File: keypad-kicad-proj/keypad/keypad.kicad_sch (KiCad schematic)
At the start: 13 parts, among them J1 Screw_Terminal_01x02, J2 USB4105-GF-A, U1 ESP32-S3-WROOM-1, U2 TLV75901PDRVT

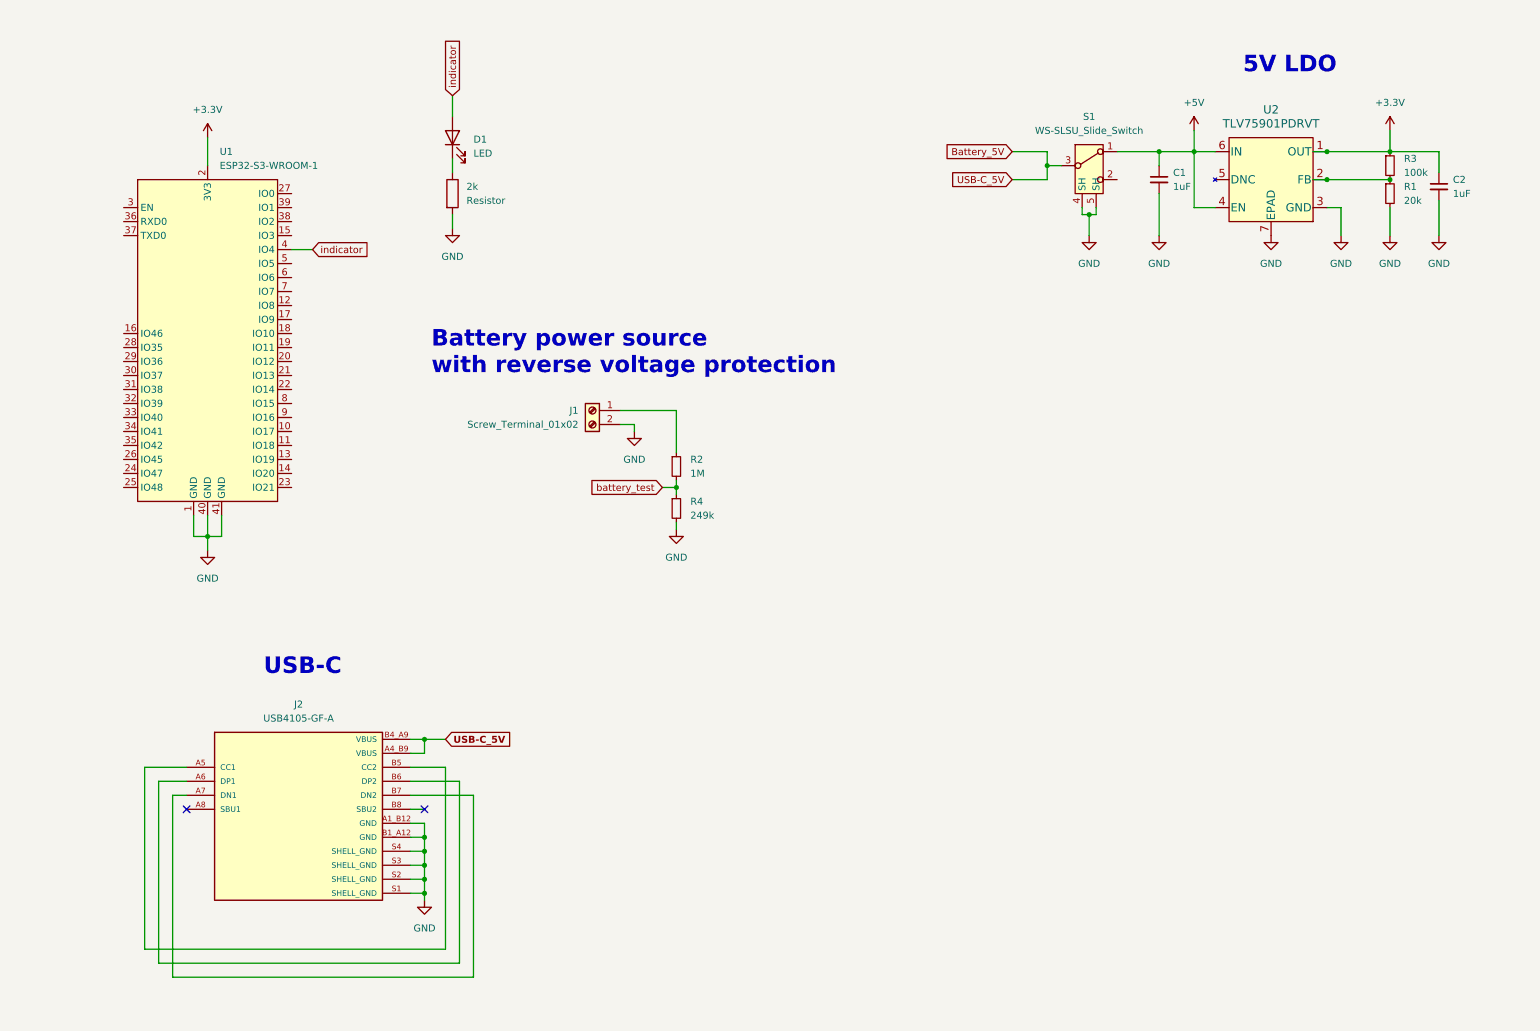
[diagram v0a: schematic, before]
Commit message: add btn matrix & led strip
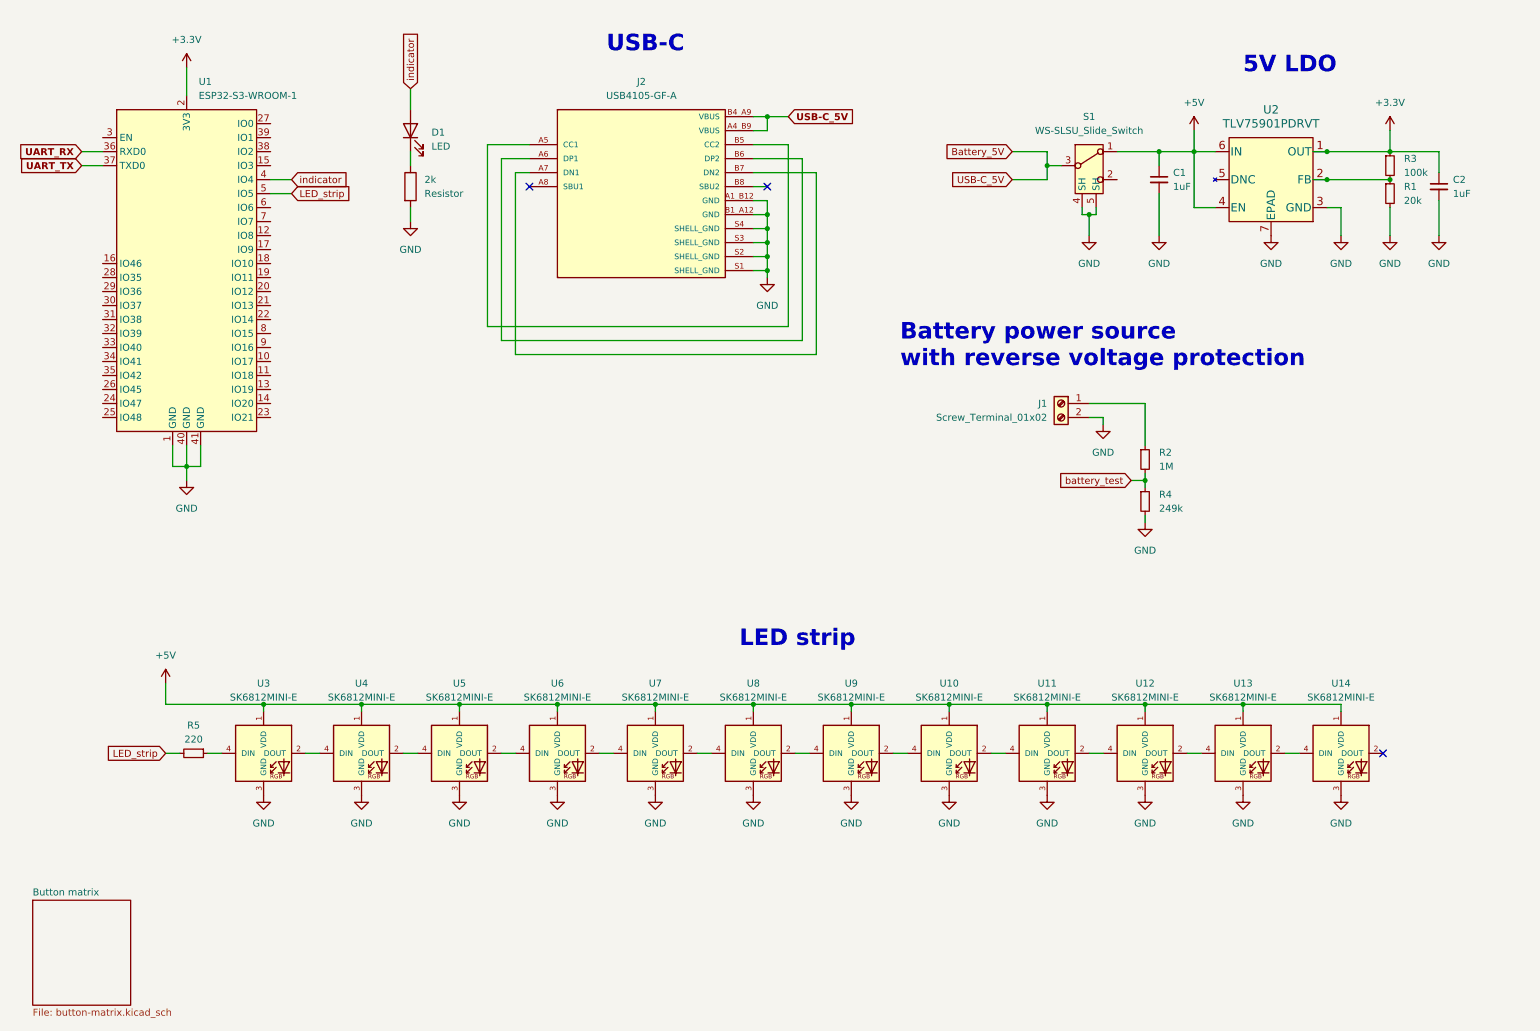
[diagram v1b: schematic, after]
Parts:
- added R5: 220, symbol PutRocketLab_RCL:R_Small
- added U10, U11, U12, U13, U14, U3, U4, U5, U6, U7, U8, U9: SK6812MINI-E, symbol PUT_RocketLab_misc:SK6812MINI-E
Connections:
- net +5V: now also U10.1 (VDD), U11.1 (VDD), U12.1 (VDD), U13.1 (VDD), U14.1 (VDD), U3.1 (VDD), U4.1 (VDD), U5.1 (VDD), U6.1 (VDD), U7.1 (VDD), U8.1 (VDD), U9.1 (VDD)
- net GND: now also U10.3 (GND), U11.3 (GND), U12.3 (GND), U13.3 (GND), U14.3 (GND), U3.3 (GND), U4.3 (GND), U5.3 (GND), U6.3 (GND), U7.3 (GND), U8.3 (GND), U9.3 (GND)
- net UART_RX: now reaches U1.36 (RXD0)
- net UART_TX: now reaches U1.37 (TXD0)
- net LED_strip: now reaches U1.5 (IO5)
- net LED_strip: now also R5.2
- new net: U10.4 (DIN), U9.2 (DOUT)
- new net: U8.2 (DOUT), U9.4 (DIN)
- new net: U7.2 (DOUT), U8.4 (DIN)
- new net: U6.2 (DOUT), U7.4 (DIN)
- new net: U13.2 (DOUT), U14.4 (DIN)
- new net: U12.2 (DOUT), U13.4 (DIN)
- new net: U4.2 (DOUT), U5.4 (DIN)
- new net: U3.2 (DOUT), U4.4 (DIN)
- new net: U5.2 (DOUT), U6.4 (DIN)
- new net: R5.1, U3.4 (DIN)
- new net: U10.2 (DOUT), U11.4 (DIN)
- new net: U11.2 (DOUT), U12.4 (DIN)
- no-connect marks 2 -> 3
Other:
- added sheet Button matrix (button-matrix.kicad_sch)
- note added: "LED strip"
- moved on the sheet: 2k, D1, J1, J2, R2, R4, U1

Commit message: add usb-c interface
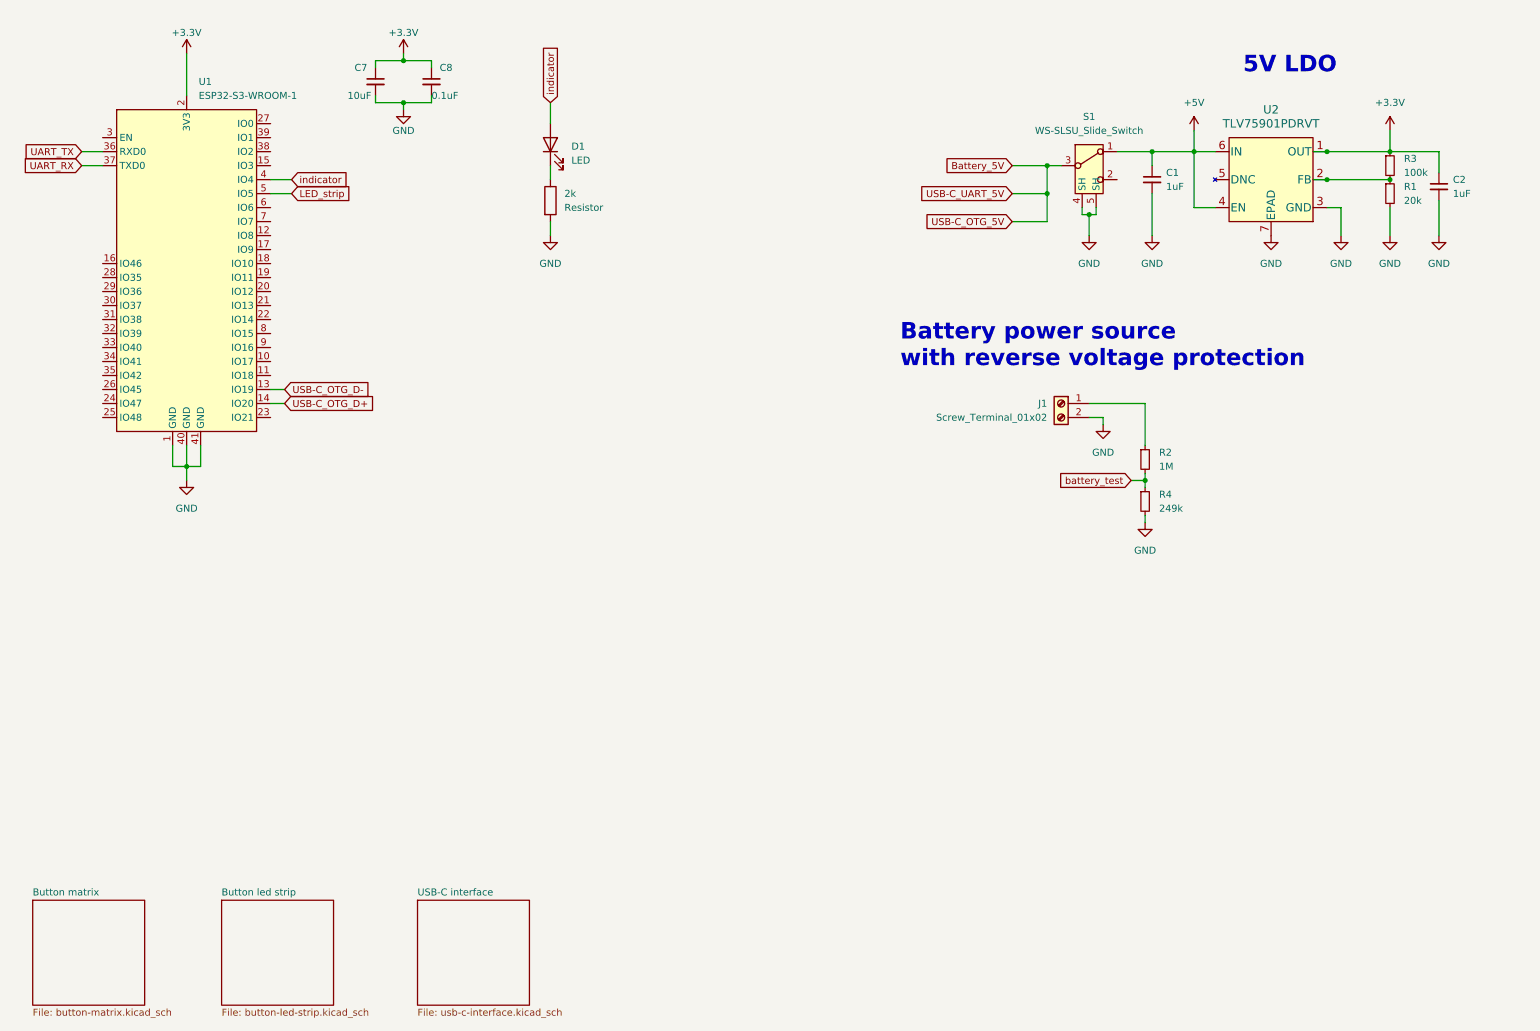
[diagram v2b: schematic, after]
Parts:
- removed J2: USB4105-GF-A, PUTRocketLab_other:GCT_USB4105-GF-A, symbol PUT_RocketLab_connectors:USB4105-GF-A
- removed R5: 220, symbol PutRocketLab_RCL:R_Small
- removed U10, U11, U12, U13, U14, U3, U4, U5, U6, U7, U8, U9: SK6812MINI-E, symbol PUT_RocketLab_misc:SK6812MINI-E
- added C7: 10uF, symbol PutRocketLab_RCL:C_Small
- added C8: 0.1uF, symbol PutRocketLab_RCL:C_Small
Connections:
- net +3V3: now also C7.1, C8.1
- net GND: now also C7.2, C8.2
- net UART_RX: now also U1.37 (TXD0); no longer U1.36 (RXD0)
- net UART_TX: now also U1.36 (RXD0); no longer U1.37 (TXD0)
- net USB-C_OTG_D-: now reaches U1.13 (IO19)
- net USB-C_OTG_D+: now reaches U1.14 (IO20)
- no-connect marks 3 -> 0
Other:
- added sheet Button led strip (button-led-strip.kicad_sch)
- added sheet USB-C interface (usb-c-interface.kicad_sch)
- note removed: "LED strip"
- note removed: "USB-C"
- moved on the sheet: 2k, C1, D1

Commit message: battery source
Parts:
- added D7: D_Small, symbol Device:D_Small
- added Q3: IRF9393TRPBF, SOIC127P600X175-8N, symbol PUTRocketLab_semiconductors:IRF9393TRPBF
- added R12: 100k, symbol PutRocketLab_RCL:R_Small
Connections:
- net Battery_5V: now also D7.1 (K), Q3.8 (D_4)
- net GND: now also R12.2
- net DTR: now reaches U1.27 (IO0)
- net RTS: now reaches U1.3 (EN)
- net at J1.1 (Pin_1), R2.1: now also Q3.1 (S_1)
- new net: D7.2 (A), Q3.4 (G), R12.1
- no-connect marks 0 -> 6
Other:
- moved on the sheet: 2k, C1, C2, D1, J1, R1, R2, R3, R4, S1, U1, U2

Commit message: rest of the schematic
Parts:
- removed 2k: Resistor, symbol PutRocketLab_RCL:Resistor
- removed C1, C2: 1uF, symbol PutRocketLab_RCL:C_Small
- removed D1: LED, symbol PUTRocketLab_semiconductors:LED
- removed D7: D_Small, symbol Device:D_Small
- removed J1: Screw_Terminal_01x02, symbol Connector:Screw_Terminal_01x02
- removed Q3: IRF9393TRPBF, SOIC127P600X175-8N, symbol PUTRocketLab_semiconductors:IRF9393TRPBF
- removed R1: 20k, symbol PutRocketLab_RCL:R_Small
- removed R12, R3: 100k, symbol PutRocketLab_RCL:R_Small
- removed R2: 1M, symbol PutRocketLab_RCL:R_Small
- removed R4: 249k, symbol PutRocketLab_RCL:R_Small
- removed S1: WS-SLSU_Slide_Switch, symbol PUT_RocketLab_connectors:WS-SLSU_Slide_Switch
- removed U2: TLV75901PDRVT, DRV6_1X1P6_TEX, symbol PUT_RocketLab_IC:TLV75901PDRVT
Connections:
- net rotary_encoder_1A: now reaches U1.12 (IO8)
- net rotary_encoder_1B: now reaches U1.17 (IO9)
- net rotary_encoder_2A: now reaches U1.18 (IO10)
- net rotary_encoder_2B: now reaches U1.19 (IO11)
- net slide_potentiometer: now reaches U1.20 (IO12)
- net SD_DET: now reaches U1.26 (IO45)
- net SD_CS: now reaches U1.32 (IO39)
- net SD_MOSI: now reaches U1.33 (IO40)
- net SD_CLK: now reaches U1.34 (IO41)
- net SD_MISO: now reaches U1.35 (IO42)
- net LCD_I2C_SCL: now reaches U1.38 (IO2)
- net LCD_I2C_SDA: now reaches U1.39 (IO1)
- net buzzer: now reaches U1.6 (IO6)
- no-connect marks 6 -> 0
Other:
- removed sheet Button led strip
- removed sheet Button matrix
- added sheet IO (io.kicad_sch)
- added sheet Micro SD connector (micro-sd-connector.kicad_sch)
- added sheet Power source (power-source.kicad_sch)
- note removed: "5V LDO"
- note removed: "Battery power source with reverse voltage protection"
- title: (none) -> Keypad board
- moved on the sheet: C7, U1

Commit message: keypad update
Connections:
- net row_0: now reaches U1.16 (IO46)
- net col_0: now reaches U1.21 (IO13)
- net col_1: now reaches U1.22 (IO14)
- net row_1: now reaches U1.28 (IO35)
- net row_2: now reaches U1.29 (IO36)
- net col_2: now reaches U1.8 (IO15)
- net col_3: now reaches U1.9 (IO16)
- no-connect marks 0 -> 9
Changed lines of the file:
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@@
   (junction (at 140.97 118.11) (diameter 0) (color 0 0 0 0)
   )
+  (no_connect (at 156.21 101.6))
+  (no_connect (at 156.21 63.5))
+  (no_connect (at 156.21 109.22))
+  (no_connect (at 125.73 106.68))
+  (no_connect (at 125.73 91.44))
+  (no_connect (at 156.21 99.06))
+  (no_connect (at 156.21 73.66))
+  (no_connect (at 125.73 88.9))
+  (no_connect (at 125.73 109.22))
   (wire (pts (xy 138.43 114.3) (xy 138.43 118.11))
     (stroke (width 0) (type default))
@@
     (stroke (width 0) (type default))
   )
+  (wire (pts (xy 124.46 86.36) (xy 125.73 86.36))
+    (stroke (width 0) (type default))
+  )
+  (wire (pts (xy 157.48 93.98) (xy 156.21 93.98))
+    (stroke (width 0) (type default))
+  )
   (wire (pts (xy 140.97 40.64) (xy 140.97 41.91))
     (stroke (width 0) (type default))
@@
     (stroke (width 0) (type default))
   )
+  (wire (pts (xy 157.48 96.52) (xy 156.21 96.52))
+    (stroke (width 0) (type default))
+  )
   (wire (pts (xy 156.21 68.58) (xy 157.48 68.58))
     (stroke (width 0) (type default))
@@
     (stroke (width 0) (type default))
   )
+  (wire (pts (xy 124.46 83.82) (xy 125.73 83.82))
+    (stroke (width 0) (type default))
+  )
+  (wire (pts (xy 157.48 91.44) (xy 156.21 91.44))
+    (stroke (width 0) (type default))
+  )
   (wire (pts (xy 137.16 41.91) (xy 140.97 41.91))
     (stroke (width 0) (type default))
@@
     (stroke (width 0) (type default))
   )
+  (wire (pts (xy 157.48 88.9) (xy 156.21 88.9))
+    (stroke (width 0) (type default))
+  )
   (wire (pts (xy 157.48 55.88) (xy 156.21 55.88))
     (stroke (width 0) (type default))
@@
     (stroke (width 0) (type default))
   )
+  (wire (pts (xy 124.46 81.28) (xy 125.73 81.28))
+    (stroke (width 0) (type default))
+  )
   (global_label "buzzer" (shape output) (at 157.48 71.12 0) (fields_autoplaced)
     (effects (font (size 1.27 1.27)) (justify left))
@@
     )
   )
+  (global_label "row_0" (shape output) (at 124.46 81.28 180) (fields_autoplaced)
+    (effects (font (size 1.27 1.27)) (justify right))
+    (property "Intersheetrefs" "${INTERSHEET_REFS}" (at 116.032 81.28 0)
+      (effects (font (size 1.27 1.27)) (justify right) hide)
+    )
+  )
   (global_label "SD_MOSI" (shape output) (at 124.46 96.52 180) (fields_autoplaced)
     (effects (font (size 1.27 1.27)) (justify right))
@@
     )
   )
+  (global_label "col_3" (shape input) (at 157.48 96.52 0) (fields_autoplaced)
+    (effects (font (size 1.27 1.27)) (justify left))
+    (property "Intersheetrefs" "${INTERSHEET_REFS}" (at 165.5451 96.52 0)
+      (effects (font (size 1.27 1.27)) (justify left) hide)
+    )
+  )
   (global_label "rotary_encoder_2A" (shape bidirectional) (at 157.48 81.28 0) (fields_autoplaced)
     (effects (font (size 1.27 1.27)) (justify left))
@@
     )
   )
+  (global_label "col_0" (shape input) (at 157.48 88.9 0) (fields_autoplaced)
+    (effects (font (size 1.27 1.27)) (justify left))
+    (property "Intersheetrefs" "${INTERSHEET_REFS}" (at 165.5451 88.9 0)
+      (effects (font (size 1.27 1.27)) (justify left) hide)
+    )
+  )
   (global_label "SD_MISO" (shape input) (at 124.46 101.6 180) (fields_autoplaced)
     (effects (font (size 1.27 1.27)) (justify right))
@@
       (effects (font (size 1.27 1.27)) (justify right) hide)
     )
+  )
+  (global_label "col_1" (shape input) (at 157.48 91.44 0) (fields_autoplaced)
+    (effects (font (size 1.27 1.27)) (justify left))
+    (property "Intersheetrefs" "${INTERSHEET_REFS}" (at 165.5451 91.44 0)
+      (effects (font (size 1.27 1.27)) (justify left) hide)
+    )
+  )
+  (global_label "col_2" (shape input) (at 157.48 93.98 0) (fields_autoplaced)
+    (effects (font (size 1.27 1.27)) (justify left))
+    (property "Intersheetrefs" "${INTERSHEET_REFS}" (at 165.5451 93.98 0)
+      (effects (font (size 1.27 1.27)) (justify left) hide)
+    )
+  )
+  (global_label "row_2" (shape output) (at 124.46 86.36 180) (fields_autoplaced)
+    (effects (font (size 1.27 1.27)) (justify right))
+    (property "Intersheetrefs" "${INTERSHEET_REFS}" (at 116.032 86.36 0)
+      (effects (font (size 1.27 1.27)) (justify right) hide)
+    )
+  )
+  (global_label "row_1" (shape output) (at 124.46 83.82 180) (fields_autoplaced)
+    (effects (font (size 1.27 1.27)) (justify right))
+    (property "Intersheetrefs" "${INTERSHEET_REFS}" (at 116.032 83.82 0)
+      (effects (font (size 1.27 1.27)) (justify right) hide)
+    )

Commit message: footprints
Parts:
- C7: footprint (none) -> Capacitor_SMD:C_0402_1005Metric
- C8: footprint (none) -> Capacitor_SMD:C_0201_0603Metric
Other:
- note added: "uC pinout"
- moved on the sheet: C7, C8, U1

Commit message: add all footprints & move libs to project specific
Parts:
- U1: footprint PUTRocketLab_IC:ESP32-S3-WROOM-1 -> RF_Module:ESP32-S3-WROOM-1
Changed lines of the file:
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@@
       (effects (font (size 1.27 1.27)) (justify left))
     )
-    (property "Footprint" "PUTRocketLab_IC:ESP32-S3-WROOM-1" (at 143.51 143.51 0)
+    (property "Footprint" "RF_Module:ESP32-S3-WROOM-1" (at 143.51 143.51 0)
       (effects (font (size 1.27 1.27)) hide)
     )

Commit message: main layout
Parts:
- C7: footprint Capacitor_SMD:C_0402_1005Metric -> Capacitor_SMD:C_0603_1608Metric
- C8: footprint Capacitor_SMD:C_0201_0603Metric -> Capacitor_SMD:C_0603_1608Metric
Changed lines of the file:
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@@
       (effects (font (size 1.27 1.27)) (justify left))
     )
-    (property "Footprint" "Capacitor_SMD:C_0201_0603Metric" (at 147.32 58.42 0)
+    (property "Footprint" "Capacitor_SMD:C_0603_1608Metric" (at 147.32 58.42 0)
       (effects (font (size 1.27 1.27)) hide)
     )
@@
       (effects (font (size 1.27 1.27)) (justify left))
     )
-    (property "Footprint" "Capacitor_SMD:C_0402_1005Metric" (at 139.7 58.42 0)
+    (property "Footprint" "Capacitor_SMD:C_0603_1608Metric" (at 139.7 58.42 0)
       (effects (font (size 1.27 1.27)) hide)
     )
